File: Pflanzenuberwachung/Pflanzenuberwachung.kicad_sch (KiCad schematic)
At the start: 0 parts

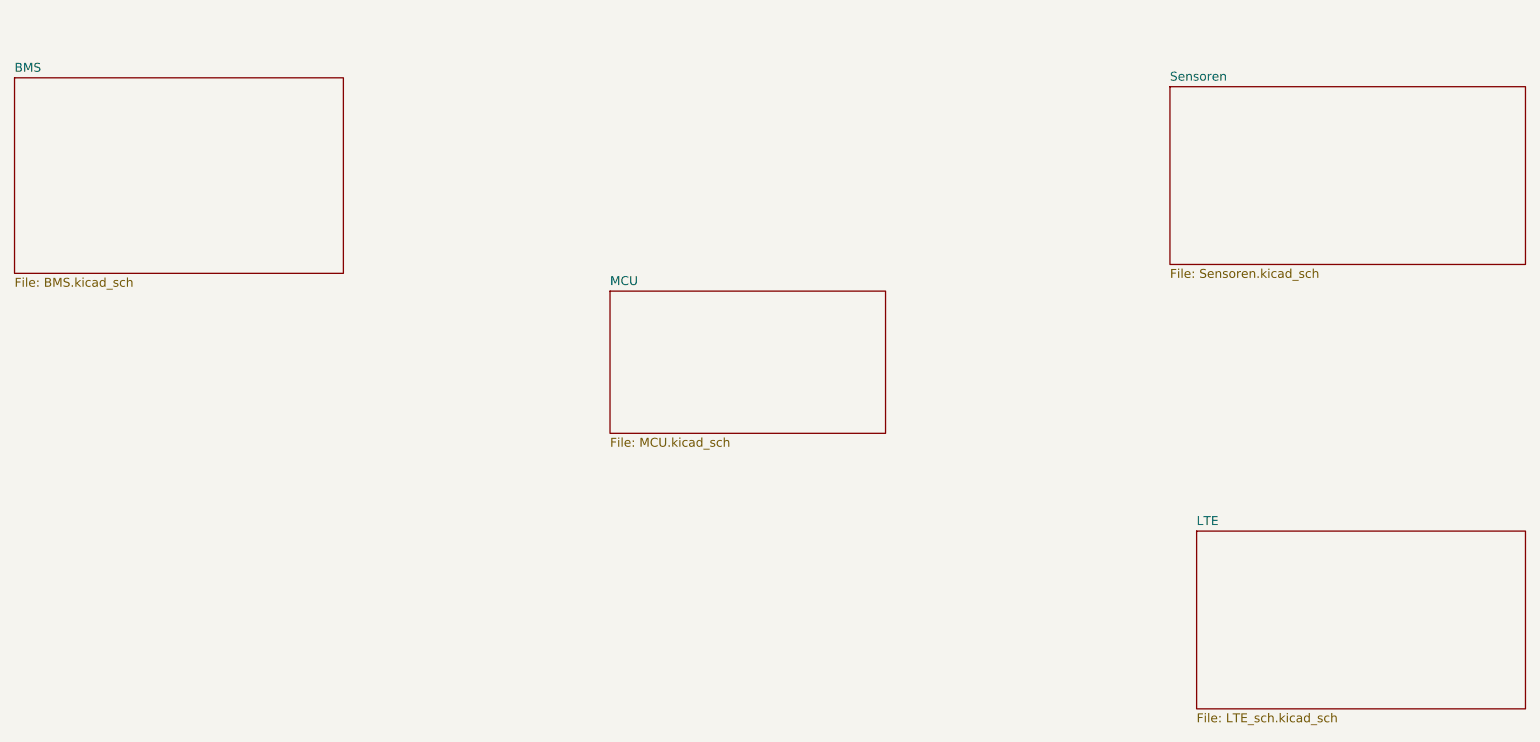
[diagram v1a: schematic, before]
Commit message: Verbindungen hinzugefügt
Microprozessor mit LTE modul  und Sensoren verbungen. Plus Statusleuchte Spannungsversorgung hinzugefügt
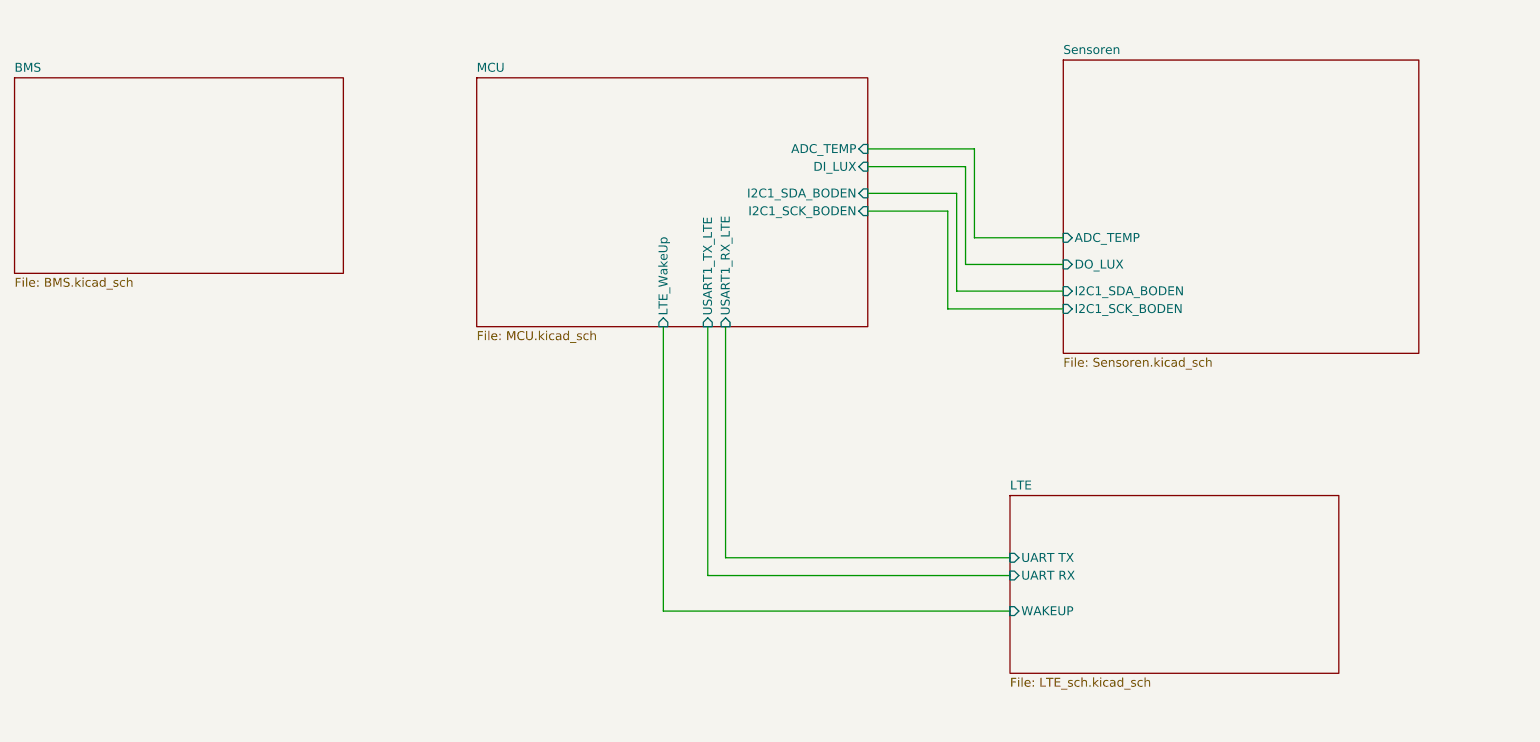
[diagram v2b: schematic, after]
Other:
- sheet LTE ports: added UART RX, UART TX, WAKEUP; removed none
- sheet MCU ports: added ADC_TEMP, DI_LUX, I2C1_SCK_BODEN, I2C1_SDA_BODEN, LTE_WakeUp, USART1_RX_LTE, USART1_TX_LTE; removed none
- sheet Sensoren ports: added ADC_TEMP, DO_LUX, I2C1_SCK_BODEN, I2C1_SDA_BODEN; removed none

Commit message: MOSFED Sensoren hinzugefügt
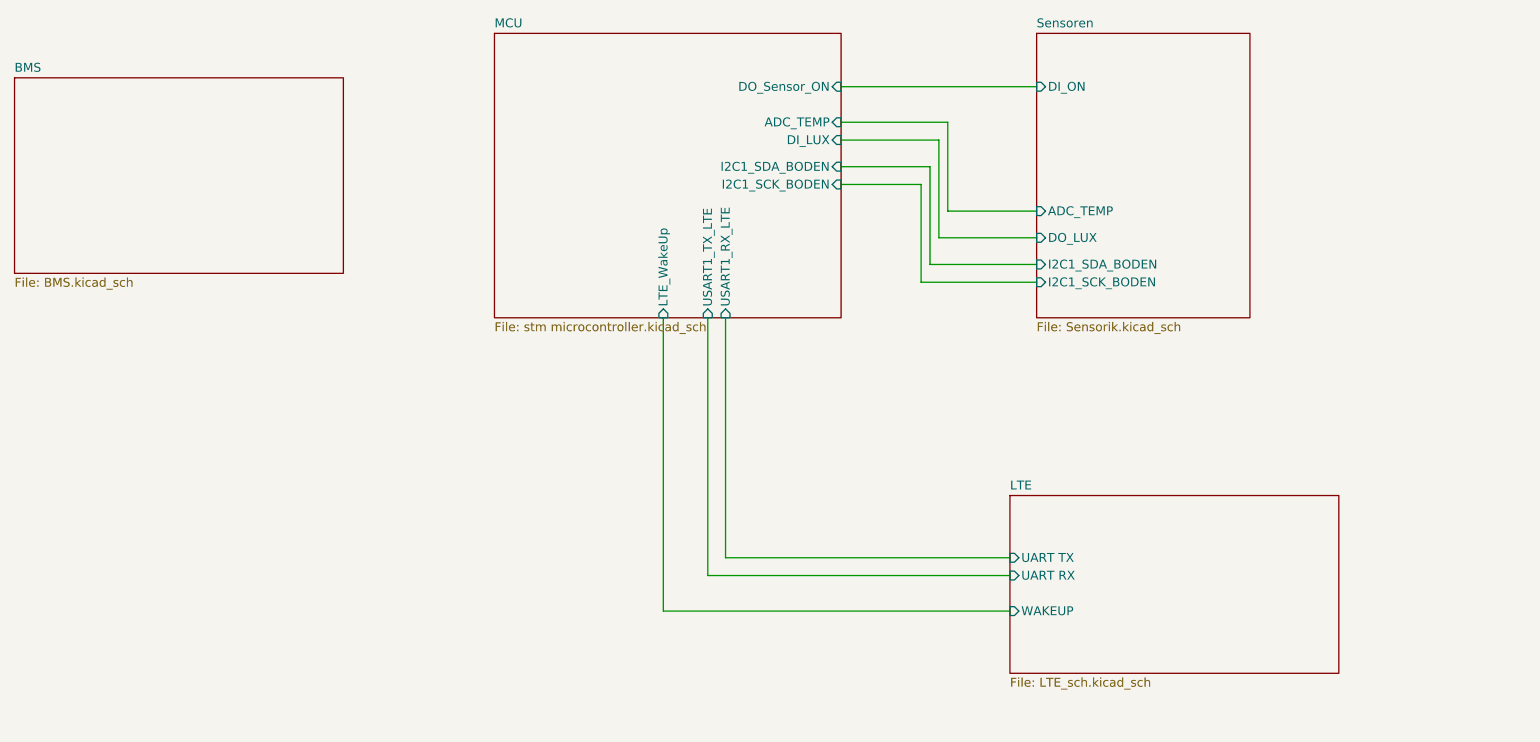
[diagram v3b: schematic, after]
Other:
- sheet MCU: file MCU.kicad_sch -> stm microcontroller.kicad_sch
- sheet MCU ports: added DO_Sensor_ON; removed none
- sheet Sensoren: file Sensoren.kicad_sch -> Sensorik.kicad_sch
- sheet Sensoren ports: added DI_ON; removed none
